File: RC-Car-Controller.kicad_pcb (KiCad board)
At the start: 4 copper layers, 107 x 72 mm, 96 parts, among them J1 USB_C_Receptacle_USB2.0, J10 JTAG, J11 UART, J2 Power_Input, J3 Conn_01x11_Socket, J4 MOTOR_1_OUTPUT, J5 MOTOR_2_OUTPUT, J6 MOTOR_3_OUTPUT, J7 MOTOR_4_OUTPUT, J8 Conn_01x03_Socket, J9 Conn_01x11_Socket, SW2 SW_Push, SW4 SW_Push, U1 LMR14020SDDAR, U10 DRV8874PWPR, U11 DRV8874PWPR, U2 SPX3819M5-L-3-3, U3 USBLC6-2SC6, U4 ESP32-S3-WROOM-1, U5 DRV8874PWPR, U9 DRV8874PWPR, X3 32.768KHz

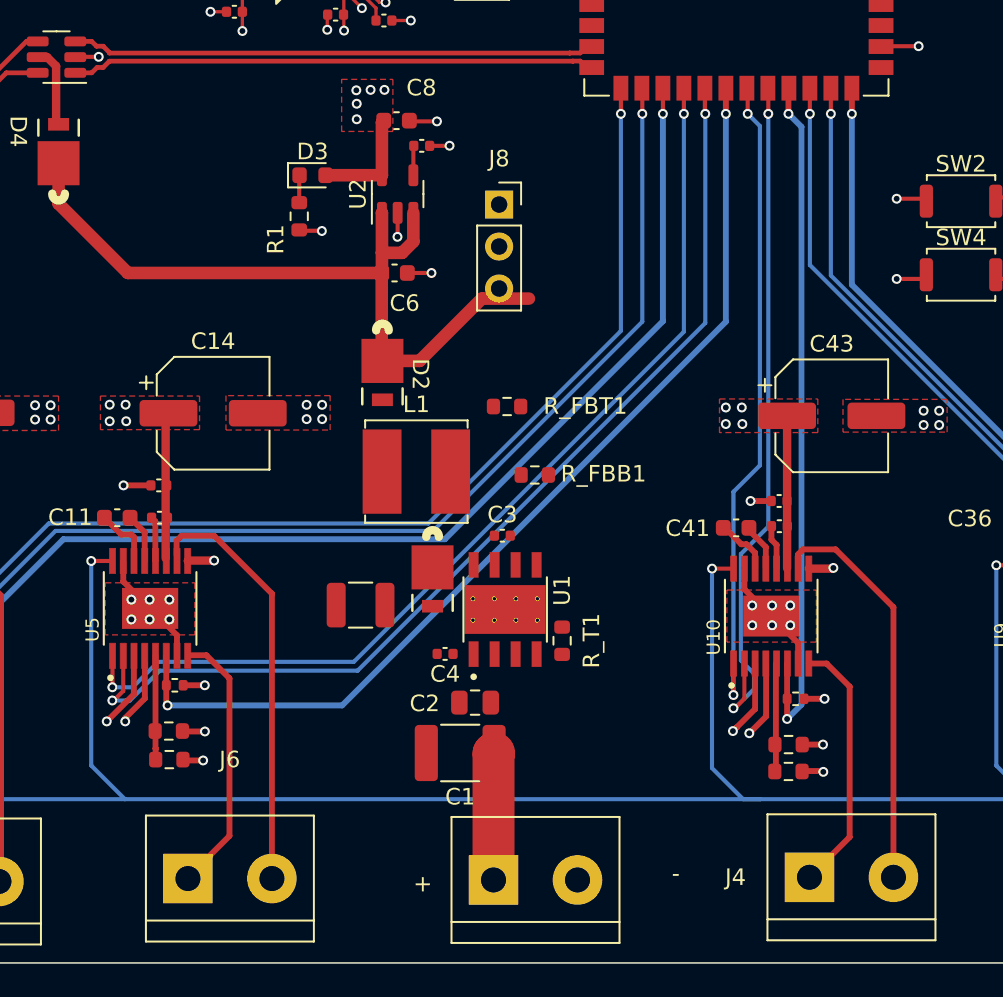
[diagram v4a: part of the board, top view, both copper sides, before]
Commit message: Update capacitor footprints
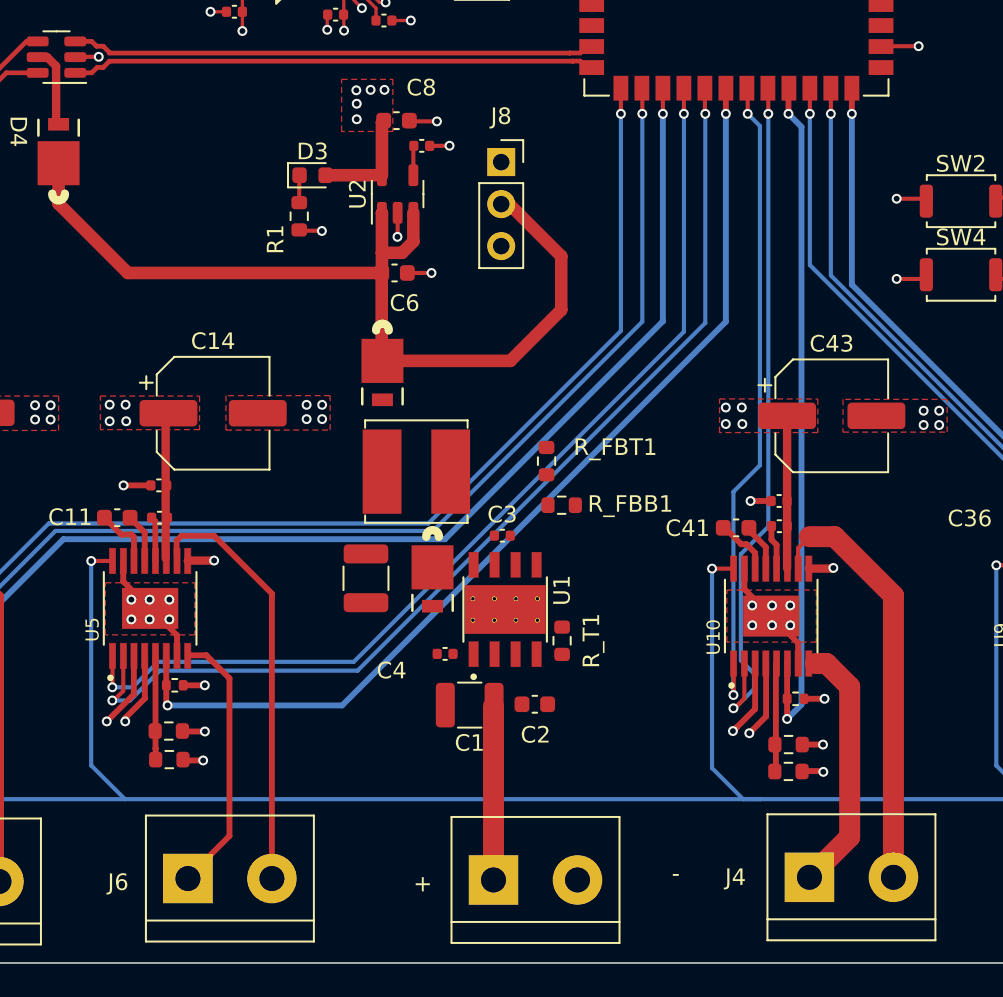
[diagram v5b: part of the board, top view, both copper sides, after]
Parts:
- C1: value 4.7u/100v -> 10u/100v; footprint Capacitor_SMD:C_1812_4532Metric -> Capacitor_SMD:C_1210_3225Metric
- C2: footprint Capacitor_SMD:C_0805_2012Metric -> Capacitor_SMD:C_0603_1608Metric
- R_T1: value 30k -> 23.7k
- moved R_FBT1 4.07 mm to (102.1, 61.6), turned to 90 degrees
- moved C2 3.61 mm to (101.4, 76.4), turned to 0 degrees
- moved C1 2.95 mm to (97.5, 76.4)
- moved J8 2.57 mm to (99.4, 43.6)
- moved R_FBB1 2.45 mm to (103.0, 64.3)
- moved C5 1.66 mm to (91.2, 68.7), turned to -90 degrees
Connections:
- U10 pad 17: (no net) -> GND
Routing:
- net +5V: track 47.0 -> 56.9 mm
- net +36V: track 45.8 -> 48.3 mm
- net MOTOR_2_OUT_2: track 24.5 -> 25.8 mm

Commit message: pcb updates & improvements
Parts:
- added JP2: MOTOR_PMODE, Jumper:SolderJumper-3_P2.0mm_Open_TrianglePad1.0x1.5mm, F.Cu at (35.2, 38.7)
- added JP3: MGN_SDA, Jumper:SolderJumper-3_P2.0mm_Open_TrianglePad1.0x1.5mm, F.Cu at (35.2, 44.6)
- C19: value 100n -> 1uf
- D2: value D_Schottky -> SS2PH10
- J1: value USB_C_Receptacle_USB2.0 -> USB-C
- J8: value Conn_01x03_Socket -> PWR
- JP1: value Jumper_PMODE -> MGN_SCL; footprint Connector_PinHeader_2.54mm:PinHeader_1x03_P2.54mm_Vertical_SMD_Pin1Right -> Jumper:SolderJumper-3_P2.0mm_Open_TrianglePad1.0x1.5mm
- R1: value 1k -> 330R
- R12: value 5k1 -> 10k
- R8: value 5k1 -> 16K
- SW2: value SW_Push -> RESET
- SW4: value SW_Push -> BOOT
- moved JP1 118.4 mm to (31.2, 56.0)
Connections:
- C15 pad 1: Net-(C15-Pad1) -> /ESP32-S3 Microcontroller /ENABLE
- IMU1 pad 6: /Sensors/MGN_SDA -> /Sensors/MPU_MGN_SDA
- IMU1 pad 7: /Sensors/MGN_SCL -> /Sensors/MPU_MGN_SCL
- JP1 pad 1: +3V3 -> SDA
- JP1 pad 2: MOTOR_PMODE -> /Sensors/MGN_SCL
- JP1 pad 3: GND -> /Sensors/MPU_MGN_SDA
- R12 pad 1: +3V3 -> /ESP32-S3 Microcontroller /ENABLE
- R12 pad 2: /ESP32-S3 Microcontroller /ENABLE -> +3V3
- R8 pad 1: /ESP32-S3 Microcontroller /ENABLE -> +3V3
- R8 pad 2: Net-(C15-Pad1) -> MOTOR_NFAULT
- SW2 pad 2: Net-(C15-Pad1) -> /ESP32-S3 Microcontroller /ENABLE
- U10 pad 17: GND -> (no net)
- U10 pad 5: /Motors/PROP_VREF_1 -> /Motors/PROP_VREF_2
- U4 pad 8: /ESP32-S3 Microcontroller /XTAL_P -> unconnected-(U4-IO15-Pad8)
- U4 pad 9: /ESP32-S3 Microcontroller /XTAL_N -> unconnected-(U4-IO16-Pad9)
- U9 pad 5: /Motors/PROP_VREF_2 -> /Motors/PROP_VREF_1
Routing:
- net Net-(C15-Pad1): track 3.81 -> 0.00 mm
- net (no net): track 0.00 -> 3.81 mm
- net /ESP32-S3 Microcontroller /ENABLE: track 10.5 -> 10.1 mm, vias 2 -> 1
- net +3V3: track 54.3 -> 54.7 mm, vias 23 -> 24
